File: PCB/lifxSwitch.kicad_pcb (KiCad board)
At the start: 2 copper layers, 30.5 x 29.8 mm, 11 parts, among them J1 Conn_01x02, J2 Conn_01x02, J3 Conn_01x02_Female, SW1 SW_SPDT, U1 MCP1826S, U2 ESP-01v090

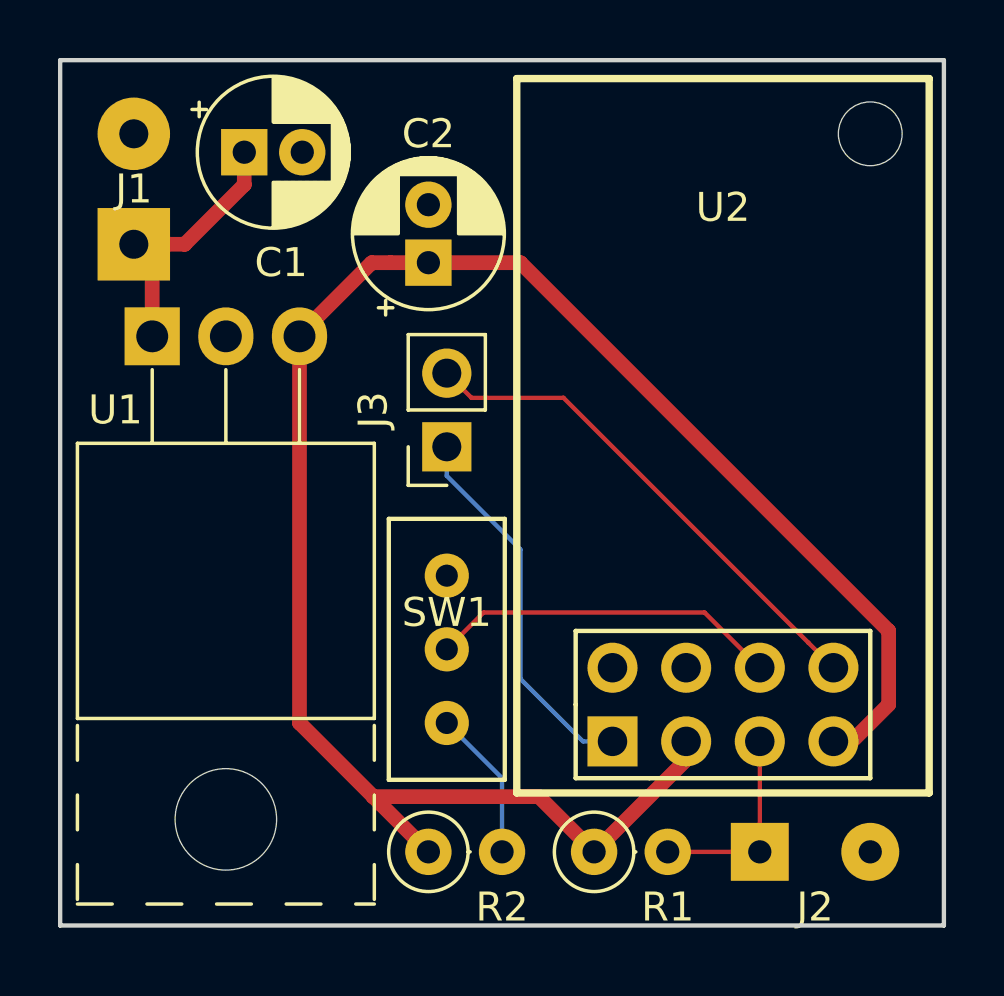
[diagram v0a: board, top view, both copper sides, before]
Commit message: Add GND header, Label RX, TX, GPIO0 switch
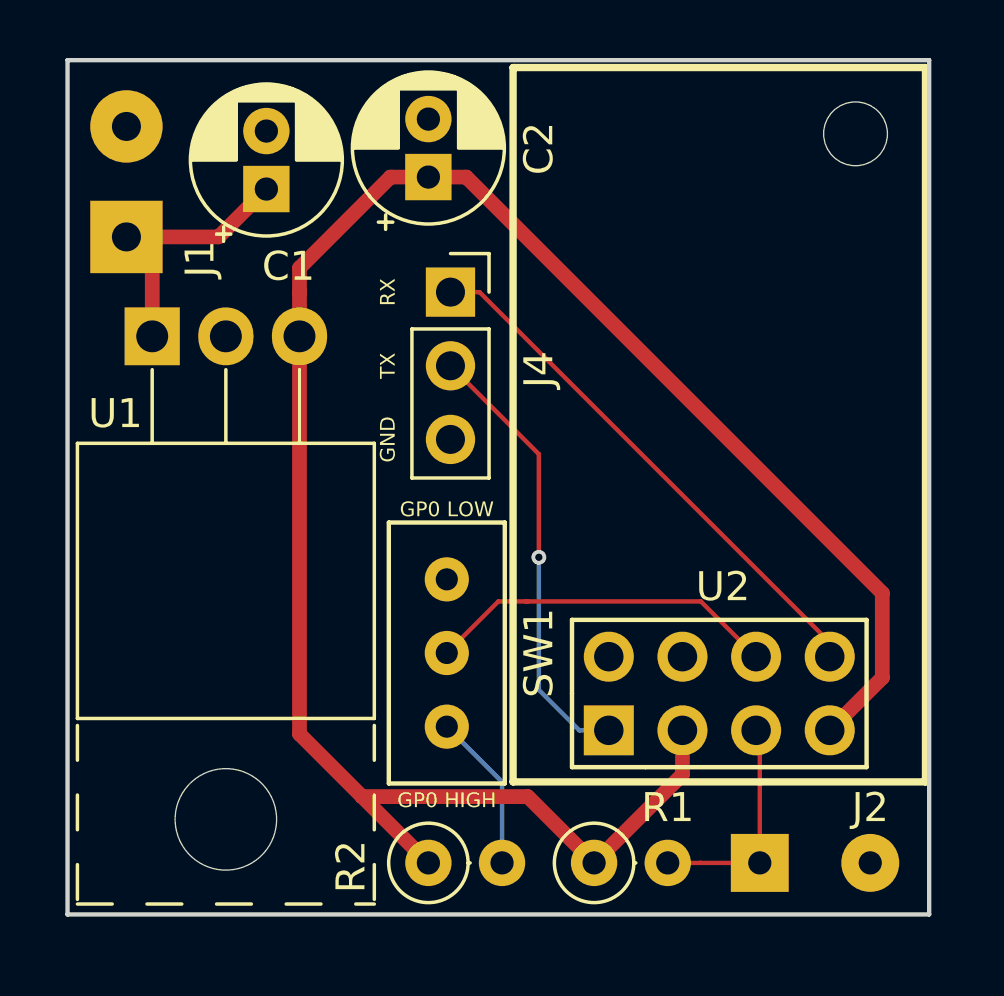
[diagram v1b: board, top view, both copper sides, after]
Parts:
- removed J3: Conn_01x02_Female, Connector_PinSocket_2.54mm:PinSocket_1x02_P2.54mm_Vertical
- added J4: Conn_01x03_Female, Connector_PinSocket_2.54mm:PinSocket_1x03_P2.54mm_Vertical, F.Cu at (126.5, 93.1)
- moved C2 2.95 mm to (125.7, 89.1)
- moved C1 1.48 mm to (120.1, 89.5), turned to 90 degrees
- moved REF** 0.51 mm to (140.5, 87.6)
- moved U2 0.40 mm to (132.0, 108.2)
- moved J2 0.38 mm to (137.2, 112.8)
- moved R1 0.38 mm to (131.4, 112.8)
- moved R2 0.38 mm to (125.7, 112.8)
- moved J1 0.36 mm to (115.3, 91.2)
- moved SW1 0.13 mm to (126.4, 105.5)
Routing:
- net +3V3: track 64.8 -> 70.0 mm
- net /TX: track 13.1 -> 15.4 mm, vias 0 -> 1
- net /RX: track 17.5 -> 18.6 mm
- net Net-(J2-Pad1): track 6.98 -> 7.80 mm
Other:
- board size 30.5 x 29.8 mm -> 29.7 x 29.5 mm
- board text added: "GND"
- board text added: "GP0 HIGH"
- board text added: "GP0 LOW"
- board text added: "RX"
- board text added: "TX"
